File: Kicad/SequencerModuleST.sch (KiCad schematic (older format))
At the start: 20 parts, among them U4 TL072

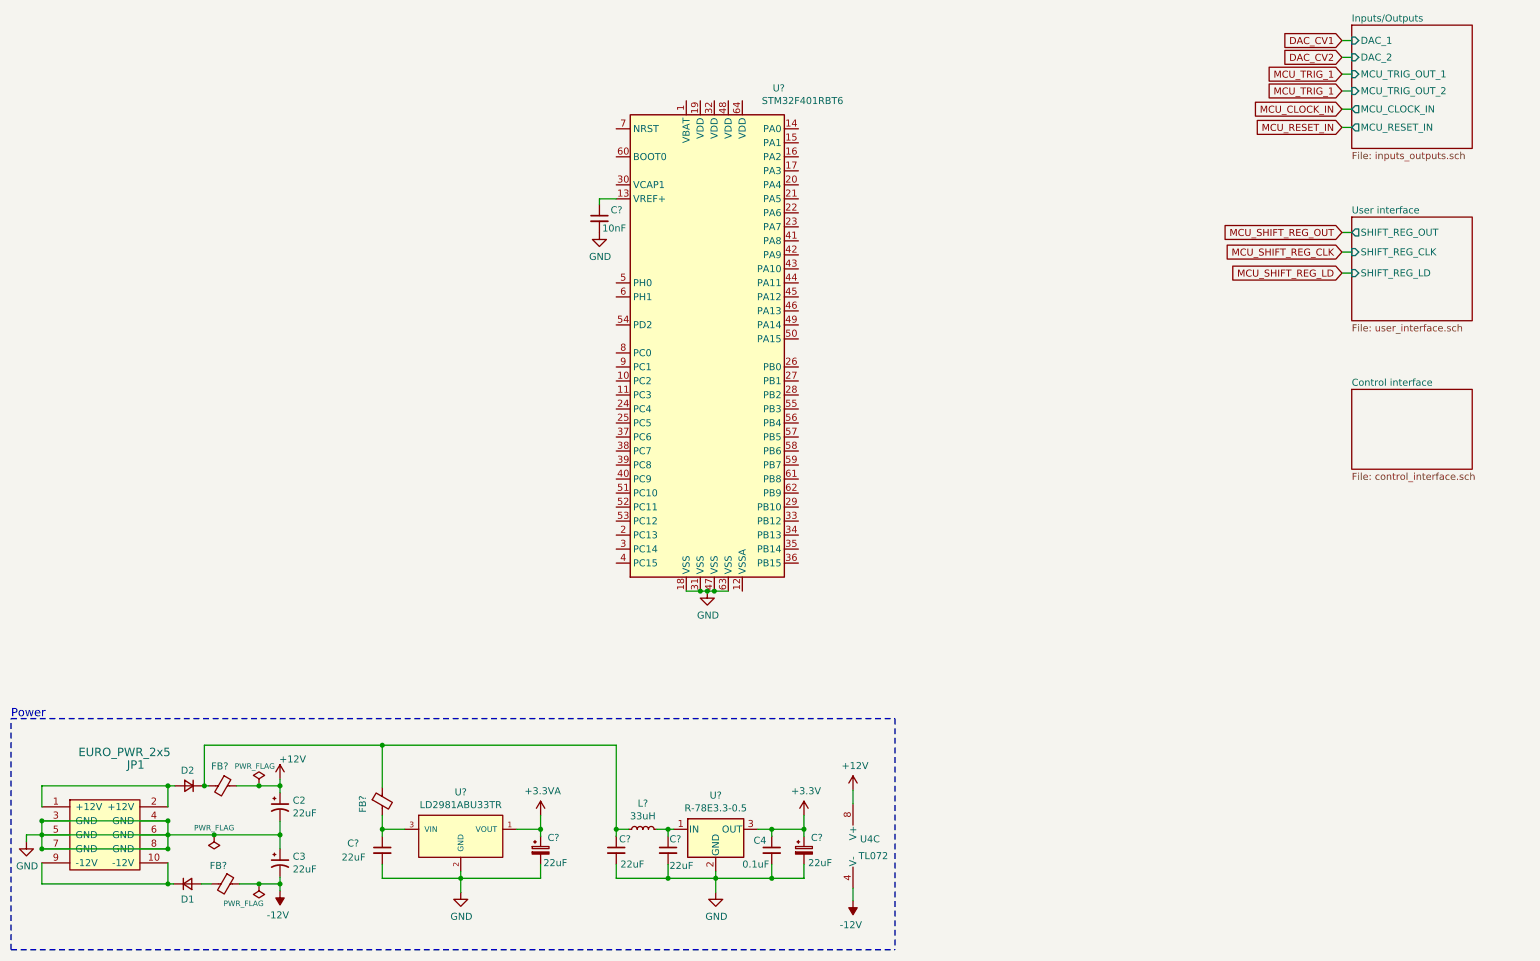
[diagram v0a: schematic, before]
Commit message: decoupling capacitors for stm32
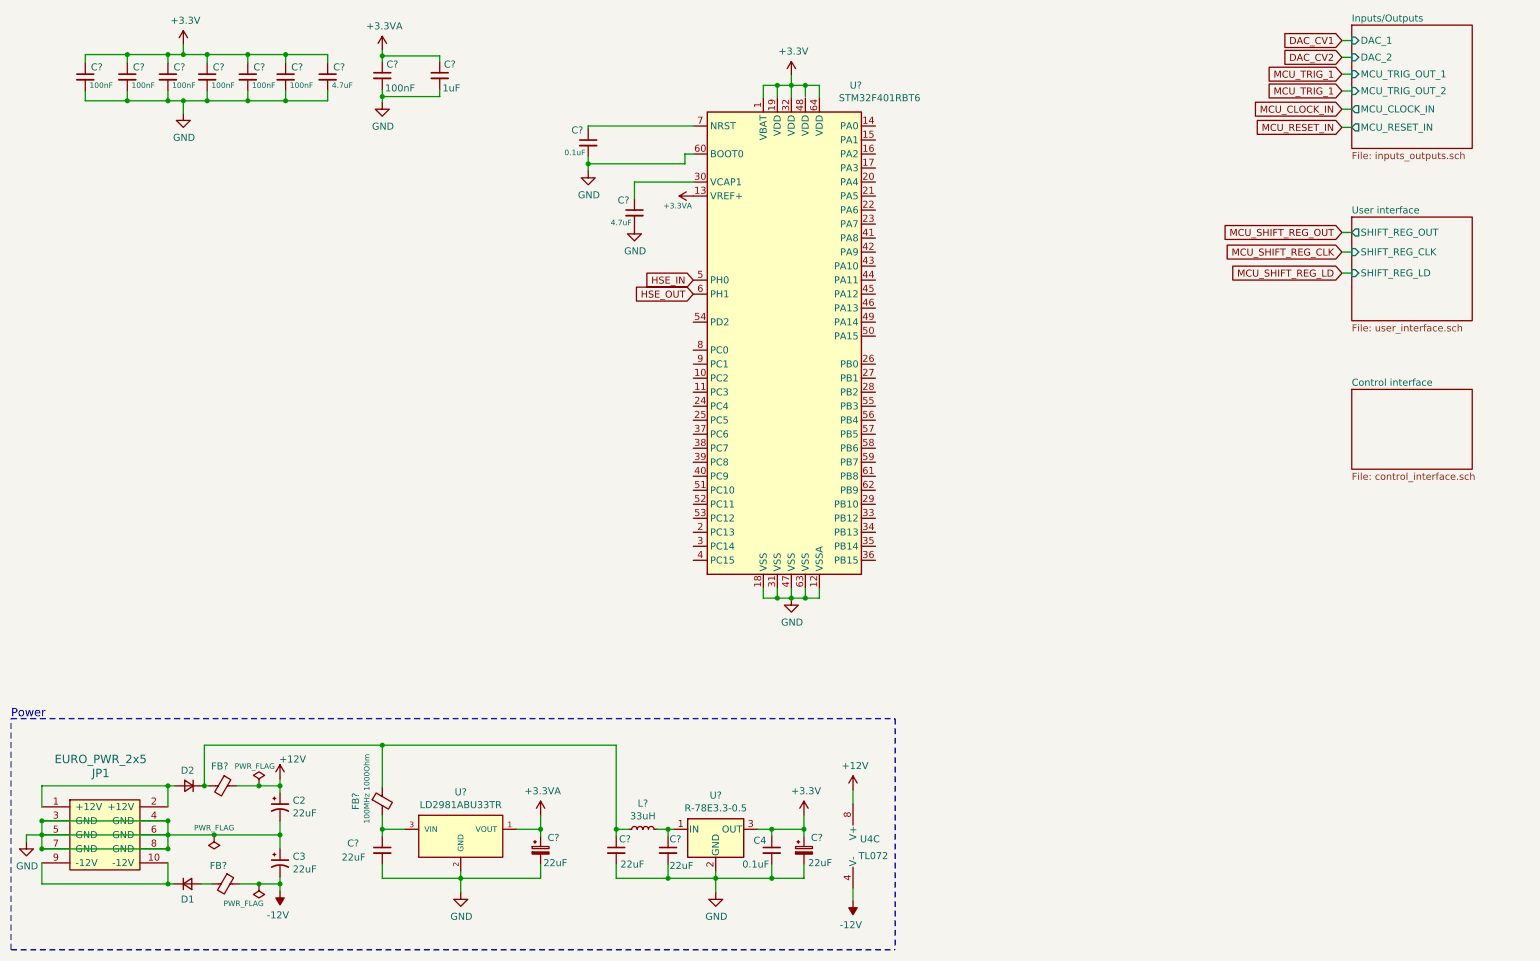
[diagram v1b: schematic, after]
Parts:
- added C? (x6): 100nF, symbol Device:C_Small
- added C? (x2): 4.7uF, symbol Device:C_Small
- added C?: 1uF, symbol Device:C_Small
- added C?: 0.1uF, symbol Device:C_Small
- C?: value 10nF -> 100nF
- FB? (x2): value Ferrite_Bead_Small -> 100MHz 1000Ohm 300mA
- FB?: value Ferrite_Bead_Small -> 100MHz 1000Ohm
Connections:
- net +3.3VA: now also C?.1, U?.13 (VREF+), C?.1
- net +3V3: now also U?.1 (VBAT), U?.19 (VDD), U?.32 (VDD), U?.64 (VDD), C?.1, C?.1, C?.1, C?.1, C?.1, C?.1, C?.1
- net GND: now also U?.12 (VSSA), U?.60 (BOOT0), C?.2, C?.2, C?.2, C?.2, C?.2, C?.2, C?.2, C?.2, C?.2, C?.2
- net at U?.30 (VCAP1): now also C?.1
- net HSE_IN: now reaches U?.5 (PH0)
- net HSE_OUT: now reaches U?.6 (PH1)
- net at U?.7 (NRST): now also C?.1
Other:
- moved on the sheet: C?, U?

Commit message: adding SWD
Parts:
- added C? (x2): 28pF, symbol Device:C_Small
- added HSE: 8MHz, symbol Device:Crystal_GND24_Small
- added J?: SWD, symbol Connector_Generic:Conn_02x05_Odd_Even
- added R?: 100, symbol Device:R_Small
- added R?: 10k, symbol Device:R_Small
- gave numbers to parts that had none: 1
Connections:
- net +3V3: now also J?.1 (Pin_1)
- net GND: now also C?.2, C?.2, HSE.2, HSE.4, J?.3 (Pin_3), J?.5 (Pin_5), J?.9 (Pin_9), R?.1; no longer U1.60 (BOOT0)
- net HSE_IN: now also C?.1, HSE.1
- net HSE_OUT: now also R?.1
- net NRST: now reaches C?.1, U1.7 (NRST)
- net NRST: now also J?.10 (Pin_10)
- new net: C?.1, HSE.3, R?.2
- new net BOOT0: R?.2, U1.60 (BOOT0)
- new net SWCLK: J?.4 (Pin_4)
- new net SWDIO: J?.2 (Pin_2)
- new net SWO: J?.6 (Pin_6)
- no-connect marks 0 -> 2
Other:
- note added: "Cl = 2 * (Ccrystal - Cparasitic)\nCparasitic = capacitance of PCB, usually 2-4pF\nCl = 2 * (18 - 4) = 28pF"
- note added: "add switch"
- moved on the sheet: C?
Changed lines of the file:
@@
 Connection ~ 1710 6430
 $Comp
-L MCU_ST_STM32F4:STM32F401RBTx U?
+L MCU_ST_STM32F4:STM32F401RBTx U1
 U 1 1 5FCBFD96
 P 6160 3220
-F 0 "U?" H 6620 5010 50  0000 C CNN
+F 0 "U1" H 6620 5010 50  0000 C CNN
 F 1 "STM32F401RBT6" H 6790 4920 50  0000 C CNN
 F 2 "Package_QFP:LQFP-64_10x10mm_P0.5mm" H 5560 1520 50  0001 R CNN
@@
 L Device:C_Small C?
 U 1 1 5FFC75D4
-P 4710 1840
-F 0 "C?" H 4590 1930 50  0000 L CNN
-F 1 "0.1uF" H 4540 1770 39  0000 L CNN
-F 2 "" H 4710 1840 50  0001 C CNN
-F 3 "~" H 4710 1840 50  0001 C CNN
-	1    4710 1840
-	1    0    0    -1
-$EndComp
-Wire Wire Line
-	4710 1740 4710 1720
-Wire Wire Line
-	4710 1720 5460 1720
+P 1580 4750
+F 0 "C?" H 1460 4840 50  0000 L CNN
+F 1 "0.1uF" H 1410 4680 39  0000 L CNN
+F 2 "" H 1580 4750 50  0001 C CNN
+F 3 "~" H 1580 4750 50  0001 C CNN
+	1    1580 4750
+	1    0    0    -1
+$EndComp
 $Comp
 L power:GND #PWR?
 U 1 1 5FFCDE46
-P 4710 2040
-F 0 "#PWR?" H 4710 1790 50  0001 C CNN
-F 1 "GND" H 4715 1867 50  0000 C CNN
-F 2 "" H 4710 2040 50  0001 C CNN
-F 3 "" H 4710 2040 50  0001 C CNN
-	1    4710 2040
-	1    0    0    -1
-$EndComp
-Wire Wire Line
-	4710 1940 4710 1990
+P 1580 4950
+F 0 "#PWR?" H 1580 4700 50  0001 C CNN
+F 1 "GND" H 1585 4777 50  0000 C CNN
+F 2 "" H 1580 4950 50  0001 C CNN
+F 3 "" H 1580 4950 50  0001 C CNN
+	1    1580 4950
+	1    0    0    -1
+$EndComp
 Wire Wire Line
 	5460 1920 5400 1920
-Wire Wire Line
-	5400 1920 5400 1990
-Wire Wire Line
-	5400 1990 4710 1990
-Connection ~ 4710 1990
-Wire Wire Line
-	4710 1990 4710 2040
 Text GLabel 5460 2820 0    50   Input ~ 0
 HSE_IN
 Text GLabel 5460 2920 0    50   Input ~ 0
 HSE_OUT
+$Comp
+L Device:Crystal_GND24_Small HSE
+U 1 1 600234EF
+P 1790 2730
+F 0 "HSE" H 1620 3090 50  0000 L CNN
+F 1 "8MHz" H 1640 3020 50  0000 L CNN
+F 2 "" H 1790 2730 50  0001 C CNN
+F 3 "~" H 1790 2730 50  0001 C CNN
+	1    1790 2730
+	1    0    0    -1
+$EndComp
+Text GLabel 1410 2730 0    50   Input ~ 0
+HSE_IN
+Text GLabel 2380 2730 2    50   Input ~ 0
+HSE_OUT
+Wire Wire Line
+	1410 2730 1570 2730
+$Comp
+L power:GND #PWR?
+U 1 1 6003C349
+P 1790 3070
+F 0 "#PWR?" H 1790 2820 50  0001 C CNN
+F 1 "GND" H 1795 2897 50  0000 C CNN
+F 2 "" H 1790 3070 50  0001 C CNN
+F 3 "" H 1790 3070 50  0001 C CNN
+	1    1790 3070
+	1    0    0    -1
+$EndComp
+Wire Wire Line
+	1790 2830 1790 3010
+$Comp
+L Device:R_Small R?
+U 1 1 60063A29
+P 2200 2730
+F 0 "R?" V 2040 2710 50  0000 C CNN
+F 1 "100" V 2110 2730 50  0000 C CNN
+F 2 "" H 2200 2730 50  0001 C CNN
+F 3 "~" H 2200 2730 50  0001 C CNN
+	1    2200 2730
+	0    1    1    0
+$EndComp
+Wire Wire Line
+	1890 2730 2000 2730
+Wire Wire Line
+	2300 2730 2380 2730
+$Comp
+L Device:C_Small C?
+U 1 1 6007193C
+P 1570 2880
+F 0 "C?" H 1380 2920 50  0000 L CNN
+F 1 "28pF" H 1320 2810 50  0000 L CNN
+F 2 "" H 1570 2880 50  0001 C CNN
+F 3 "~" H 1570 2880 50  0001 C CNN
+	1    1570 2880
+	1    0    0    -1
+$EndComp
+Wire Wire Line
+	1570 2780 1570 2730
+Connection ~ 1570 2730
+Wire Wire Line
+	1570 2730 1690 2730
+Wire Wire Line
+	1570 2980 1570 3010
+Wire Wire Line
+	1570 3010 1790 3010
+Connection ~ 1790 3010
+Wire Wire Line
+	1790 3010 1790 3070
+$Comp
+L Device:C_Small C?
+U 1 1 60099F46
+P 2000 2880
+F 0 "C?" H 2110 2880 50  0000 L CNN
+F 1 "28pF" H 2050 2790 50  0000 L CNN
+F 2 "" H 2000 2880 50  0001 C CNN
+F 3 "~" H 2000 2880 50  0001 C CNN
+	1    2000 2880
+	1    0    0    -1
+$EndComp
+Wire Wire Line
+	2000 2780 2000 2730
+Connection ~ 2000 2730
+Wire Wire Line
+	2000 2730 2100 2730
+Wire Wire Line
+	2000 2980 2000 3010
+Wire Wire Line
+	2000 3010 1790 3010
+Wire Wire Line
+	1790 2630 1790 2530
+Wire Wire Line
+	1790 2530 1000 2530
+Wire Wire Line
+	1000 2530 1000 3010
+Wire Wire Line
+	1000 3010 1570 3010
+Connection ~ 1570 3010
+Text Notes 940  3600 0    50   ~ 0
+Cl = 2 * (Ccrystal - Cparasitic)\nCparasitic = capacitance of PCB, usually 2-4pF\nCl = 2 * (18 - 4) = 28pF
+Wire Wire Line
+	1580 4850 1580 4950
+Text GLabel 5400 1920 0    50   Input ~ 0
+BOOT0
+Text GLabel 1160 4580 1    50   Input ~ 0
+BOOT0
+$Comp
+L Device:R_Small R?
+U 1 1 600C4176
+P 1160 4770
+F 0 "R?" V 1000 4750 50  0000 C CNN
+F 1 "10k" V 1070 4770 50  0000 C CNN
+F 2 "" H 1160 4770 50  0001 C CNN
+F 3 "~" H 1160 4770 50  0001 C CNN
+	1    1160 4770
+	-1   0    0    1
+$EndComp
+$Comp
+L power:GND #PWR?
+U 1 1 600C49A5
+P 1160 4950
+F 0 "#PWR?" H 1160 4700 50  0001 C CNN
+F 1 "GND" H 1165 4777 50  0000 C CNN
+F 2 "" H 1160 4950 50  0001 C CNN
+F 3 "" H 1160 4950 50  0001 C CNN
+	1    1160 4950
+	1    0    0    -1
+$EndComp
+Wire Wire Line
+	1160 4950 1160 4870
+Wire Wire Line
+	1160 4670 1160 4580
+Text Notes 700  4670 0    50   ~ 0
+add switch
+Text GLabel 7860 2790 0    50   Input ~ 0
+SWDIO
+Text GLabel 7870 2930 0    50   Input ~ 0
+SWCLK
+Text GLabel 7870 3100 0    50   Input ~ 0
+SWO
+$Comp
+L Connector_Generic:Conn_02x05_Odd_Even J?
+U 1 1 600D5646
+P 2830 4590
+F 0 "J?" H 2880 5007 50  0000 C CNN
+F 1 "SWD" H 2880 4916 50  0000 C CNN
+F 2 "" H 2830 4590 50  0001 C CNN
+F 3 "~" H 2830 4590 50  0001 C CNN
+	1    2830 4590
+	1    0    0    -1
+$EndComp
+$Comp
+L power:+3.3V #PWR?
+U 1 1 600D6096
+P 2630 4390
+F 0 "#PWR?" H 2630 4240 50  0001 C CNN
+F 1 "+3.3V" V 2645 4518 50  0000 L CNN
+F 2 "" H 2630 4390 50  0001 C CNN
+F 3 "" H 2630 4390 50  0001 C CNN
+	1    2630 4390
+	0    -1   -1   0
+$EndComp
+$Comp
+L power:GND #PWR?
+U 1 1 600D6D9F
+P 2530 4870
+F 0 "#PWR?" H 2530 4620 50  0001 C CNN
+F 1 "GND" H 2535 4697 50  0000 C CNN
+F 2 "" H 2530 4870 50  0001 C CNN
+F 3 "" H 2530 4870 50  0001 C CNN
+	1    2530 4870
+	1    0    0    -1
+$EndComp
+Wire Wire Line
+	2630 4490 2530 4490
+Wire Wire Line
+	2530 4490 2530 4590
+Wire Wire Line
+	2630 4590 2530 4590
+Connection ~ 2530 4590
+Wire Wire Line
+	2530 4590 2530 4790
+Wire Wire Line
+	2630 4790 2530 4790
+Connection ~ 2530 4790
+Wire Wire Line
+	2530 4790 2530 4870
+NoConn ~ 2630 4690
+NoConn ~ 3130 4690
+Text GLabel 3130 4390 2    50   Input ~ 0
+SWDIO
+Text GLabel 3130 4490 2    50   Input ~ 0
+SWCLK
+Text GLabel 5460 1720 0    50   Input ~ 0
+NRST
+Text GLabel 1580 4530 1    50   Input ~ 0
+NRST
+Wire Wire Line
+	1580 4530 1580 4650
+Text GLabel 3130 4790 2    50   Input ~ 0
+NRST
+Text GLabel 3130 4590 2    50   Input ~ 0
+SWO
 $EndSCHEMATC
